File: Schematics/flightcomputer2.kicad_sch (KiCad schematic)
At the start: 0 parts

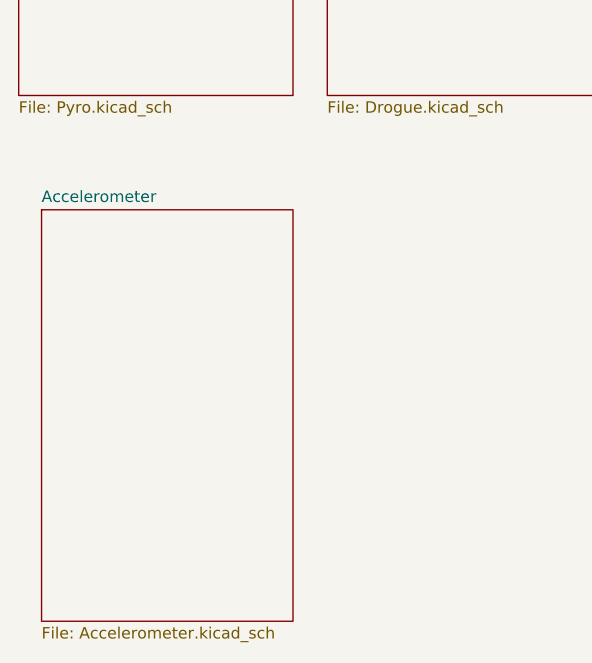
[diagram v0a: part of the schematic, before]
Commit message: added LCSC numbers and footprint values, need to connect schemeatic pins, then can start layout
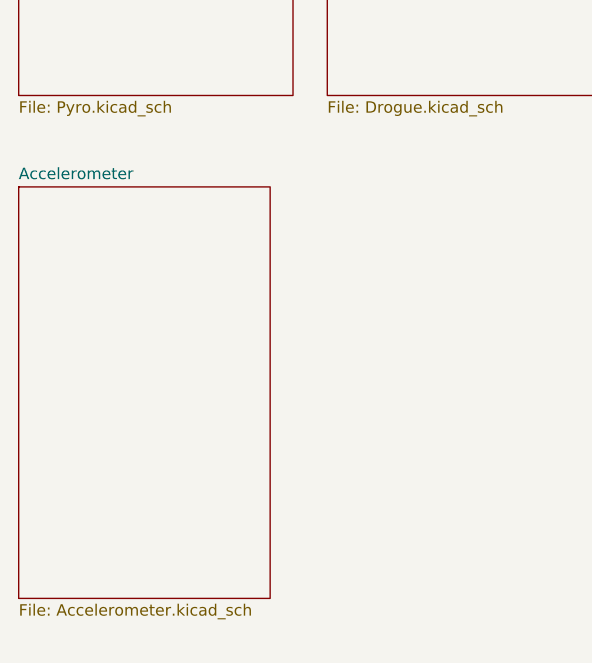
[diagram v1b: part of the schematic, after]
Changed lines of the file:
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@@
 	)
 	(sheet
-		(at 26.67 142.24)
+		(at 24.13 139.7)
 		(size 27.94 45.72)
 		(exclude_from_sim no)
@@
 		)
 		(property "Sheetname" "Accelerometer"
-			(at 26.67 141.5284 0)
+			(at 24.13 138.9884 0)
 			(effects
 				(font
@@
 		)
 		(property "Sheetfile" "Accelerometer.kicad_sch"
-			(at 26.67 188.5446 0)
+			(at 24.13 186.0046 0)
 			(effects
 				(font

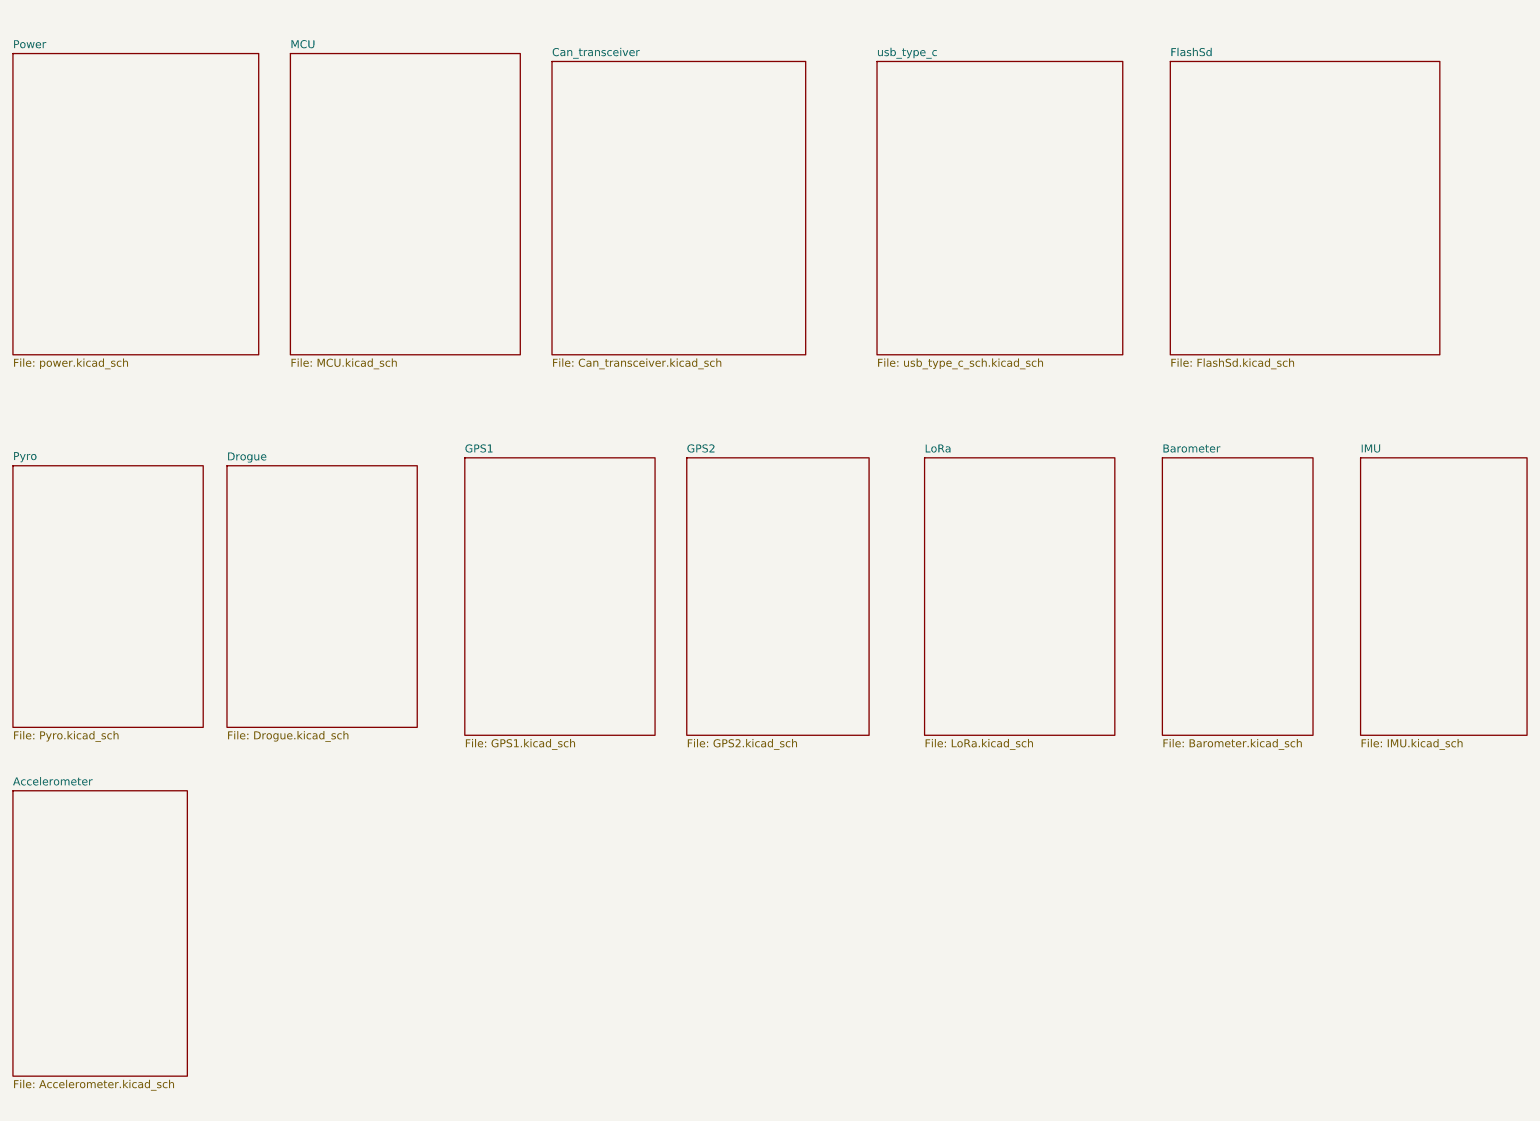
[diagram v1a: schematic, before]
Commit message: fixed symbols and added diodes to power input before ldo
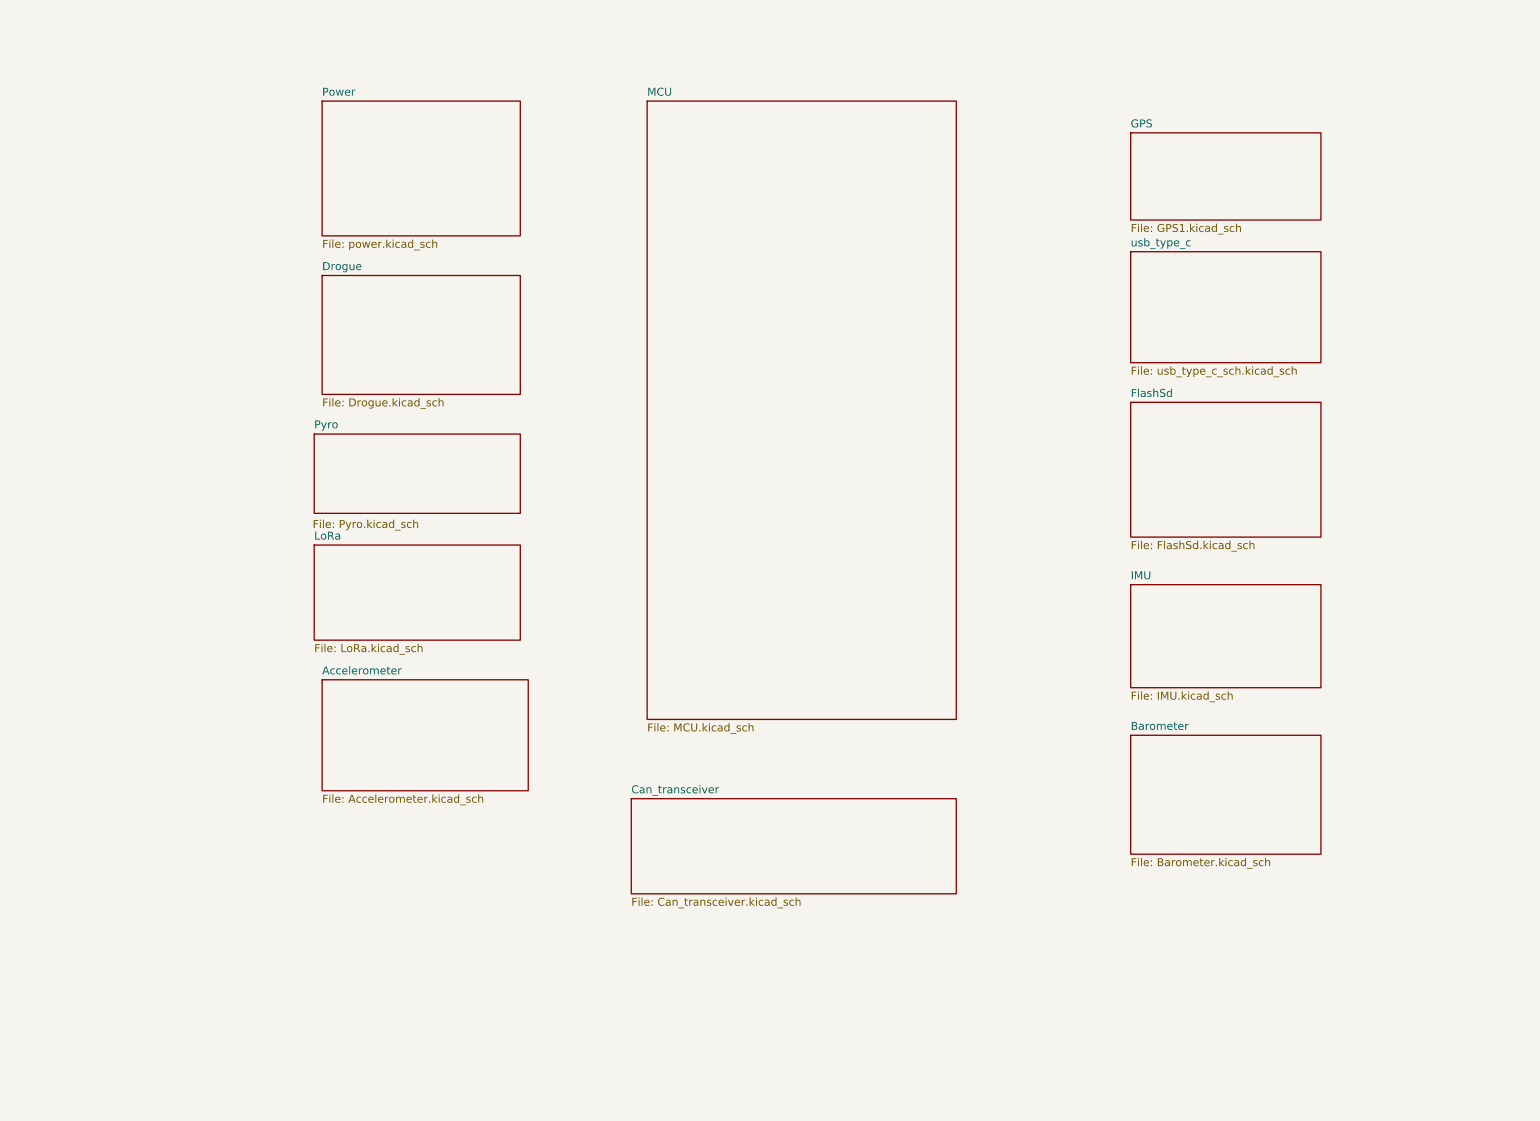
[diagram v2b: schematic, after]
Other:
- sheet GPS1 renamed GPS
- removed sheet GPS2
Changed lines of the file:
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@@
 	(paper "A4")
 	(sheet
-		(at 24.13 87.63)
-		(size 30.48 41.91)
+		(at 72.39 82.55)
+		(size 33.02 12.7)
 		(exclude_from_sim no)
 		(in_bom yes)
@@
 		)
 		(property "Sheetname" "Pyro"
-			(at 24.13 86.868 0)
+			(at 72.39 81.788 0)
 			(effects
 				(font
@@
 		)
 		(property "Sheetfile" "Pyro.kicad_sch"
-			(at 24.13 130.1246 0)
+			(at 72.136 96.266 0)
 			(effects
 				(font
@@
 	)
 	(sheet
-		(at 162.56 22.86)
-		(size 39.37 46.99)
+		(at 203.2 53.34)
+		(size 30.48 17.78)
 		(exclude_from_sim no)
 		(in_bom yes)
@@
 		)
 		(property "Sheetname" "usb_type_c"
-			(at 162.56 22.1484 0)
+			(at 203.2 52.6284 0)
 			(effects
 				(font
@@
 		)
 		(property "Sheetfile" "usb_type_c_sch.kicad_sch"
-			(at 162.56 70.4346 0)
+			(at 203.2 71.7046 0)
 			(effects
 				(font
@@
 	)
 	(sheet
-		(at 68.58 21.59)
-		(size 36.83 48.26)
+		(at 125.73 29.21)
+		(size 49.53 99.06)
 		(exclude_from_sim no)
 		(in_bom yes)
@@
 		)
 		(property "Sheetname" "MCU"
-			(at 68.58 20.8784 0)
+			(at 125.73 28.4984 0)
 			(effects
 				(font
@@
 		)
 		(property "Sheetfile" "MCU.kicad_sch"
-			(at 68.58 70.4346 0)
+			(at 125.73 128.8546 0)
 			(effects
 				(font
@@
 	)
 	(sheet
-		(at 96.52 86.36)
-		(size 30.48 44.45)
-		(exclude_from_sim no)
-		(in_bom yes)
-		(on_board yes)
-		(dnp no)
-		(fields_autoplaced yes)
-		(stroke
-			(width 0.1524)
-			(type solid)
-		)
-		(fill
-			(color 0 0 0 0.0000)
-		)
-		(property "Sheetname" "GPS1"
-			(at 96.52 85.6484 0)
+		(at 203.2 34.29)
+		(size 30.48 13.97)
+		(exclude_from_sim no)
+		(in_bom yes)
+		(on_board yes)
+		(dnp no)
+		(fields_autoplaced yes)
+		(stroke
+			(width 0.1524)
+			(type solid)
+		)
+		(fill
+			(color 0 0 0 0.0000)
+		)
+		(property "Sheetname" "GPS"
+			(at 203.2 33.5784 0)
 			(effects
 				(font
@@
 		)
 		(property "Sheetfile" "GPS1.kicad_sch"
-			(at 96.52 131.3946 0)
+			(at 203.2 48.8446 0)
 			(effects
 				(font
@@
 	)
 	(sheet
-		(at 58.42 87.63)
-		(size 30.48 41.91)
+		(at 73.66 57.15)
+		(size 31.75 19.05)
 		(exclude_from_sim no)
 		(in_bom yes)
@@
 		)
 		(property "Sheetname" "Drogue"
-			(at 58.42 86.9184 0)
+			(at 73.66 56.4384 0)
 			(effects
 				(font
@@
 		)
 		(property "Sheetfile" "Drogue.kicad_sch"
-			(at 58.42 130.1246 0)
+			(at 73.66 76.7846 0)
 			(effects
 				(font
@@
 	)
 	(sheet
-		(at 208.28 86.36)
-		(size 24.13 44.45)
+		(at 203.2 130.81)
+		(size 30.48 19.05)
 		(exclude_from_sim no)
 		(in_bom yes)
@@
 		)
 		(property "Sheetname" "Barometer"
-			(at 208.28 85.6484 0)
+			(at 203.2 130.0984 0)
 			(effects
 				(font
@@
 		)
 		(property "Sheetfile" "Barometer.kicad_sch"
-			(at 208.28 131.3946 0)
+			(at 203.2 150.4446 0)
 			(effects
 				(font
@@
 	)
 	(sheet
-		(at 110.49 22.86)
-		(size 40.64 46.99)
+		(at 123.19 140.97)
+		(size 52.07 15.24)
 		(exclude_from_sim no)
 		(in_bom yes)
@@
 		)
 		(property "Sheetname" "Can_transceiver"
-			(at 110.49 22.1484 0)
+			(at 123.19 140.2584 0)
 			(effects
 				(font
@@
 		)
 		(property "Sheetfile" "Can_transceiver.kicad_sch"
-			(at 110.49 70.4346 0)
+			(at 123.19 156.7946 0)
 			(effects
 				(font
@@
 	)
 	(sheet
-		(at 24.13 139.7)
-		(size 27.94 45.72)
+		(at 73.66 121.92)
+		(size 33.02 17.78)
 		(exclude_from_sim no)
 		(in_bom yes)
@@
 		)
 		(property "Sheetname" "Accelerometer"
-			(at 24.13 138.9884 0)
+			(at 73.66 121.2084 0)
 			(effects
 				(font
@@
 		)
 		(property "Sheetfile" "Accelerometer.kicad_sch"
-			(at 24.13 186.0046 0)
+			(at 73.66 140.2846 0)
 			(effects
 				(font
@@
 	)
 	(sheet
-		(at 170.18 86.36)
-		(size 30.48 44.45)
+		(at 72.39 100.33)
+		(size 33.02 15.24)
 		(exclude_from_sim no)
 		(in_bom yes)
@@
 		)
 		(property "Sheetname" "LoRa"
-			(at 170.18 85.6484 0)
+			(at 72.39 99.6184 0)
 			(effects
 				(font
@@
 		)
 		(property "Sheetfile" "LoRa.kicad_sch"
-			(at 170.18 131.3946 0)
+			(at 72.39 116.1546 0)
 			(effects
 				(font
@@
 	)
 	(sheet
-		(at 132.08 86.36)
-		(size 29.21 44.45)
-		(exclude_from_sim no)
-		(in_bom yes)
-		(on_board yes)
-		(dnp no)
-		(fields_autoplaced yes)
-		(stroke
-			(width 0.1524)
-			(type solid)
-		)
-		(fill
-			(color 0 0 0 0.0000)
-		)
-		(property "Sheetname" "GPS2"
-			(at 132.08 85.6484 0)
-			(effects
-				(font
-					(size 1.27 1.27)
-				)
-				(justify left bottom)
-			)
-		)
-		(property "Sheetfile" "GPS2.kicad_sch"
-			(at 132.08 131.3946 0)
-			(effects
-				(font
-					(size 1.27 1.27)
-				)
-				(justify left top)
-			)
-		)
-		(instances
-			(project "flightcomputer2"
-				(path "/6cb3dda3-5fe8-4715-b831-354360aa3199"
-					(page "9")
-				)
-			)
-		)
-	)
-	(sheet
-		(at 24.13 21.59)
-		(size 39.37 48.26)
+		(at 73.66 29.21)
+		(size 31.75 21.59)
 		(exclude_from_sim no)
 		(in_bom yes)
@@
 		)
 		(property "Sheetname" "Power"
-			(at 24.13 20.8784 0)
+			(at 73.66 28.4984 0)
 			(effects
 				(font
@@
 		)
 		(property "Sheetfile" "power.kicad_sch"
-			(at 24.13 70.4346 0)
+			(at 73.66 51.3846 0)
 			(effects
 				(font
@@
 	)
 	(sheet
-		(at 240.03 86.36)
-		(size 26.67 44.45)
+		(at 203.2 106.68)
+		(size 30.48 16.51)
 		(exclude_from_sim no)
 		(in_bom yes)
@@
 		)
 		(property "Sheetname" "IMU"
-			(at 240.03 85.6484 0)
+			(at 203.2 105.9684 0)
 			(effects
 				(font
@@
 		)
 		(property "Sheetfile" "IMU.kicad_sch"
-			(at 240.03 131.3946 0)
+			(at 203.2 123.7746 0)
 			(effects
 				(font
@@
 	)
 	(sheet
-		(at 209.55 22.86)
-		(size 43.18 46.99)
+		(at 203.2 77.47)
+		(size 30.48 21.59)
 		(exclude_from_sim no)
 		(in_bom yes)
@@
 		)
 		(property "Sheetname" "FlashSd"
-			(at 209.55 22.1484 0)
+			(at 203.2 76.7584 0)
 			(effects
 				(font
@@
 		)
 		(property "Sheetfile" "FlashSd.kicad_sch"
-			(at 209.55 70.4346 0)
-			(effects
-				(font
+			(at 203.2 99.6446 0)
+			(effects
+				(font

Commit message: added lora correct and organizing sheet pins
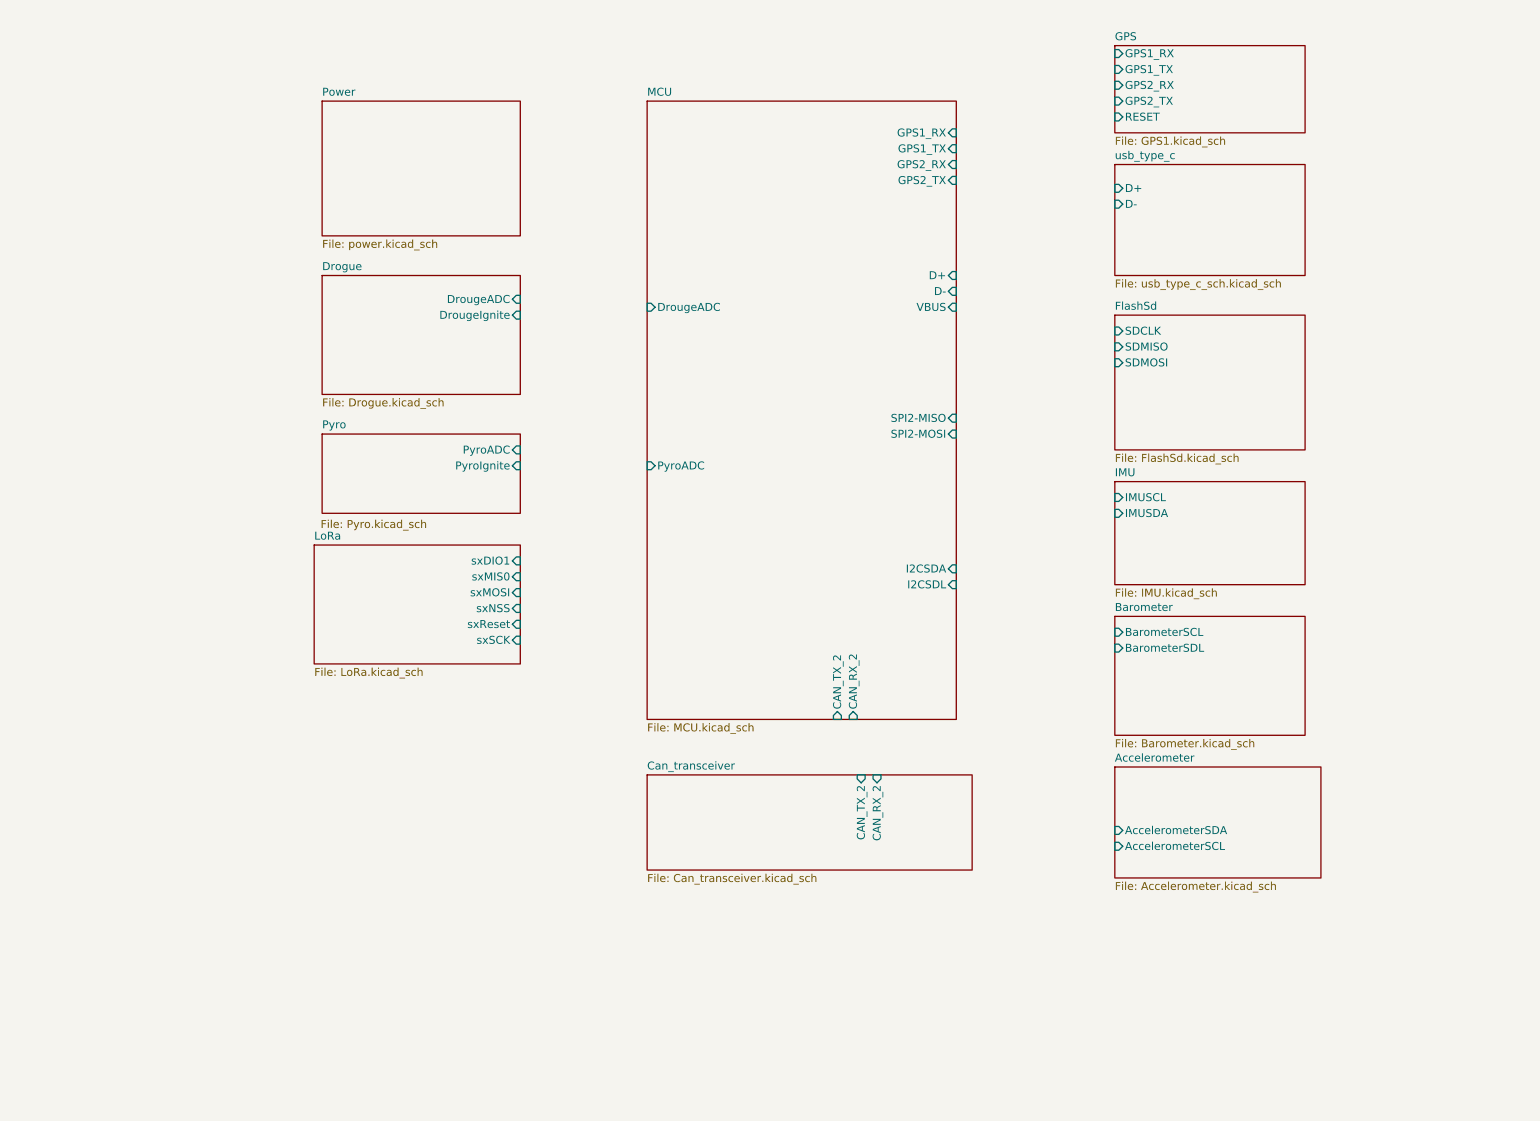
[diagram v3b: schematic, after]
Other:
- sheet Accelerometer ports: added AccelerometerSCL, AccelerometerSDA; removed none
- sheet Barometer ports: added BarometerSCL, BarometerSDL; removed none
- sheet Can_transceiver ports: added CAN_RX_2, CAN_TX_2; removed none
- sheet Drogue ports: added DrougeADC, DrougeIgnite; removed none
- sheet FlashSd ports: added SDCLK, SDMISO, SDMOSI; removed none
- sheet GPS ports: added GPS1_RX, GPS1_TX, GPS2_RX, GPS2_TX, RESET; removed none
- sheet IMU ports: added IMUSCL, IMUSDA; removed none
- sheet LoRa ports: added sxDIO1, sxMIS0, sxMOSI, sxNSS, sxReset, sxSCK; removed none
- sheet MCU ports: added CAN_RX_2, CAN_TX_2, D+, D-, DrougeADC, GPS1_RX, GPS1_TX, GPS2_RX, GPS2_TX, I2CSDA, I2CSDL, PyroADC, SPI2-MISO, SPI2-MOSI, VBUS; removed none
- sheet Pyro ports: added PyroADC, PyroIgnite; removed none
- sheet usb_type_c ports: added D+, D-; removed none
